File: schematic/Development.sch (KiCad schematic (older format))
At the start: 104 parts

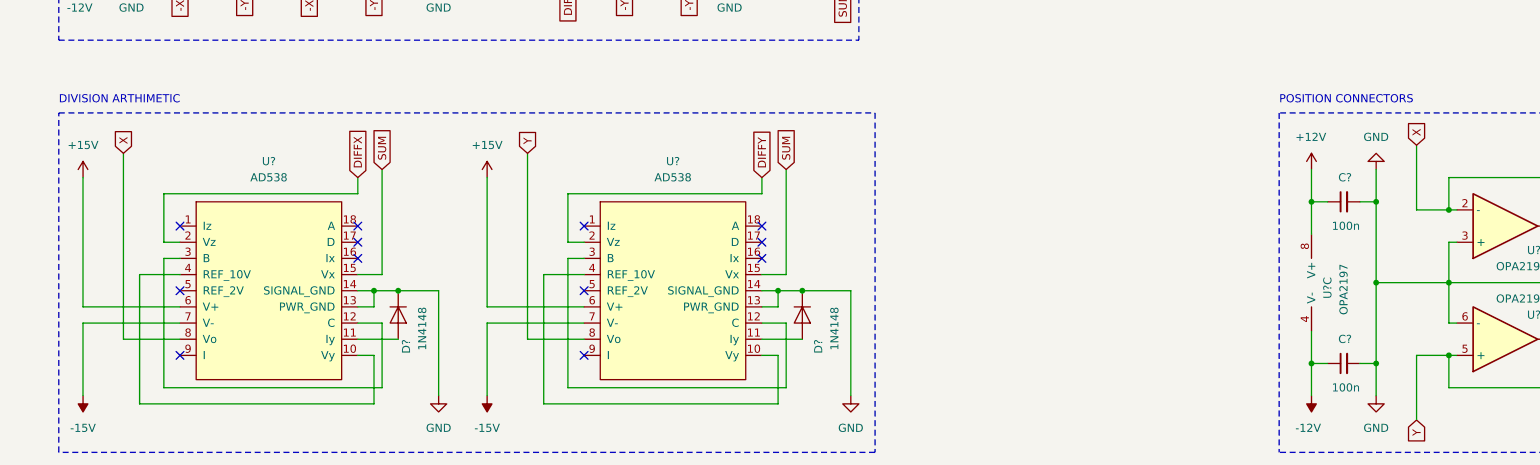
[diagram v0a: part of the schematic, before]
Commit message: renamed X,Y to POSX, POSY
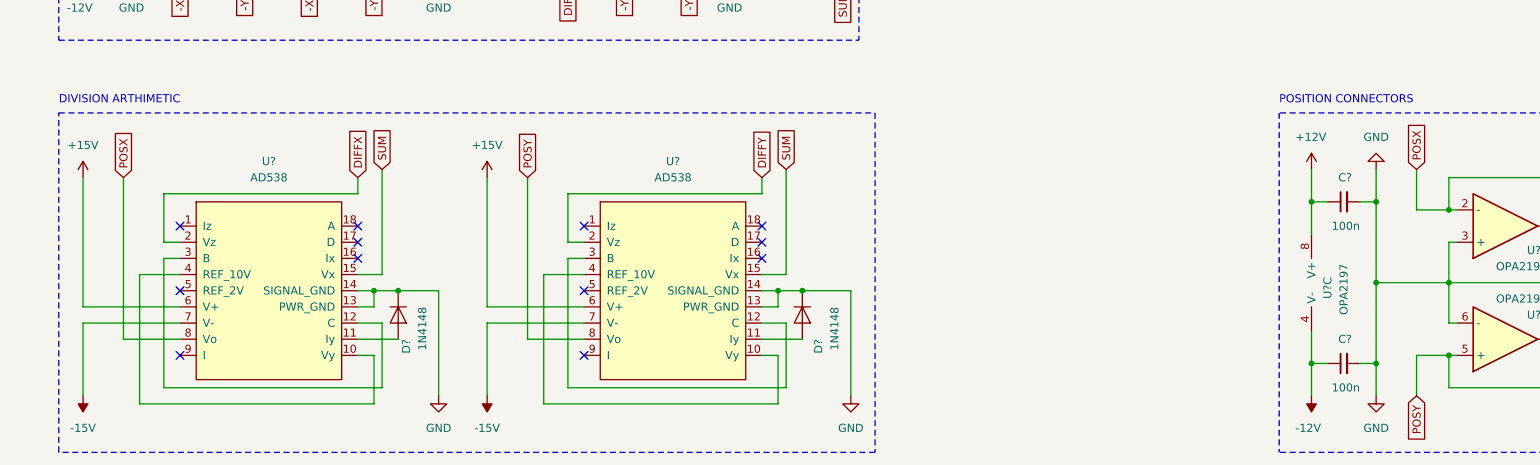
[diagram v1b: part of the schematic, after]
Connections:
- net X renamed POSX
- net Y renamed POSY
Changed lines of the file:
@@
 Wire Wire Line
 	4800 8300 4800 8600
-Text GLabel 4550 8050 1    50   Input ~ 0
-X
+Text GLabel 4550 8200 1    50   Input ~ 0
+POSX
 Wire Wire Line
 	4550 9200 4900 9200
 Wire Wire Line
-	4550 8050 4550 9200
+	4550 8200 4550 9200
 Connection ~ 6250 8900
 Wire Wire Line
@@
 Wire Wire Line
 	7300 8300 7300 8600
-Text GLabel 7050 8050 1    50   Input ~ 0
-Y
+Text GLabel 7050 8200 1    50   Input ~ 0
+POSY
 Wire Wire Line
 	7050 9200 7400 9200
 Wire Wire Line
-	7050 8050 7050 9200
+	7050 8200 7050 9200
 Connection ~ 8750 8900
 Wire Wire Line
@@
 $EndComp
 Wire Wire Line
-	12550 8400 12550 8000
+	12550 8400 12550 8150
 $Comp
 L Connector:Conn_Coaxial J?
@@
 	12550 8400 12750 8400
 Wire Wire Line
-	12550 9300 12550 9700
+	12550 9300 12550 9550
 $Comp
 L Connector:Conn_Coaxial J?
@@
 Wire Notes Line
 	15900 9900 11700 9900
-Text GLabel 12550 8000 1    50   Input ~ 0
-X
-Text GLabel 12550 9700 3    50   Input ~ 0
-Y
+Text GLabel 12550 8150 1    50   Input ~ 0
+POSX
+Text GLabel 12550 9550 3    50   Input ~ 0
+POSY
 $Comp
 L Development-rescue:Opamp_Dual_Generic-Device U?

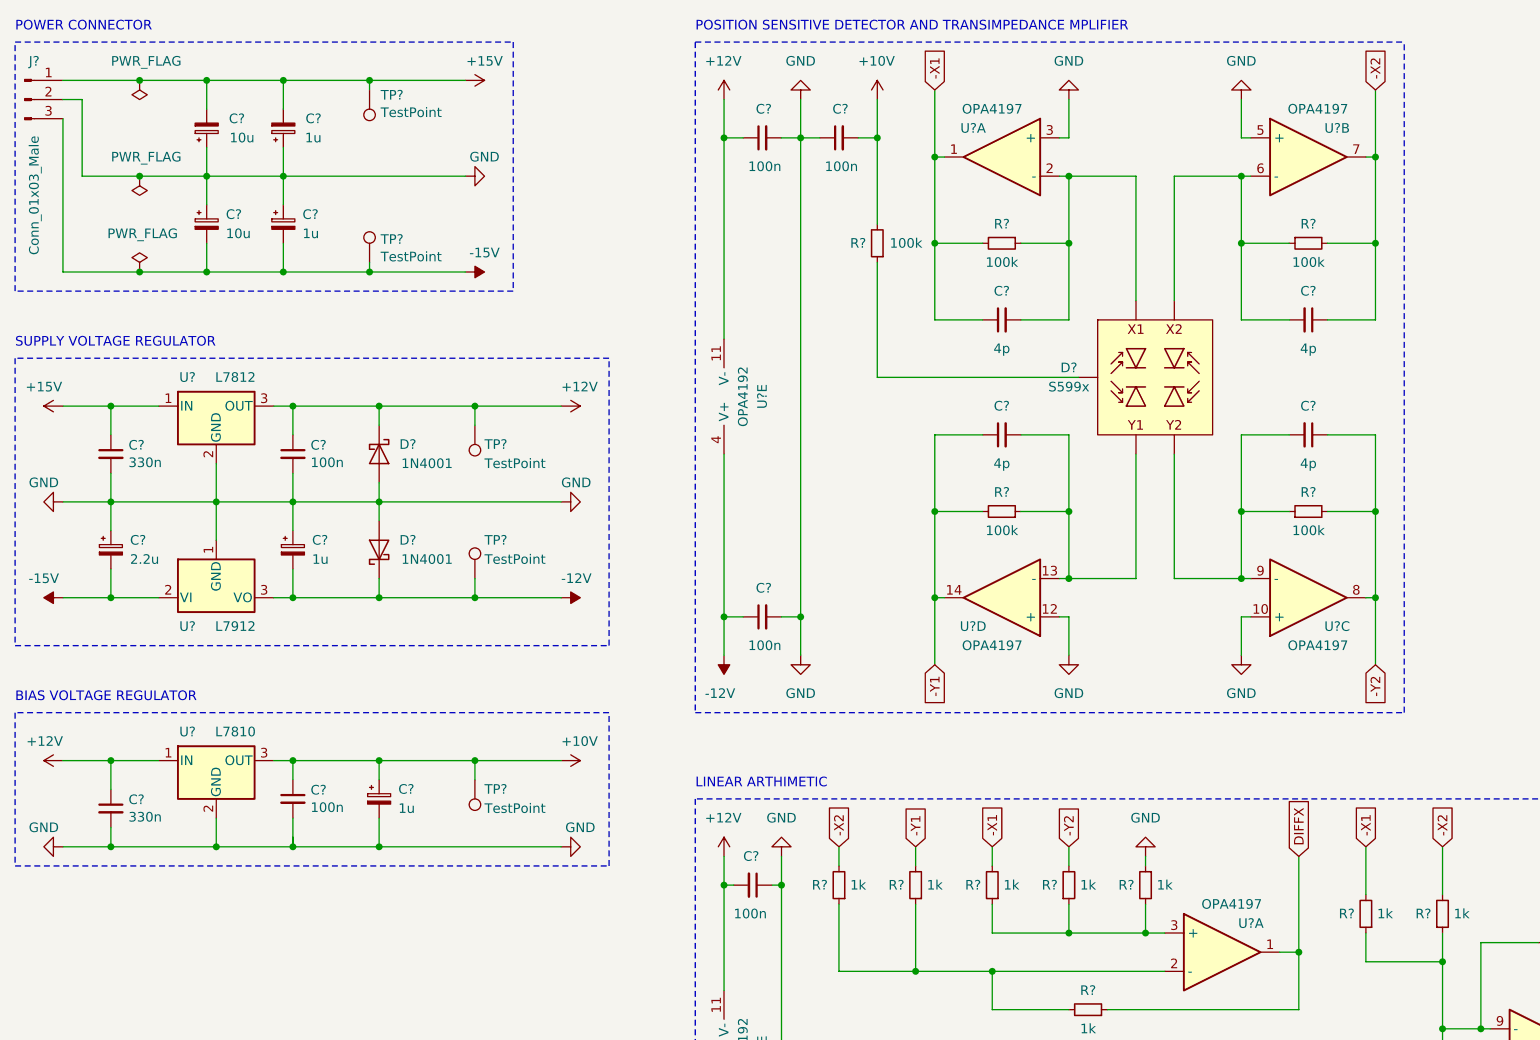
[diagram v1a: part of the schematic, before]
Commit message: replaced reverse bias voltage regulator with voltage reference
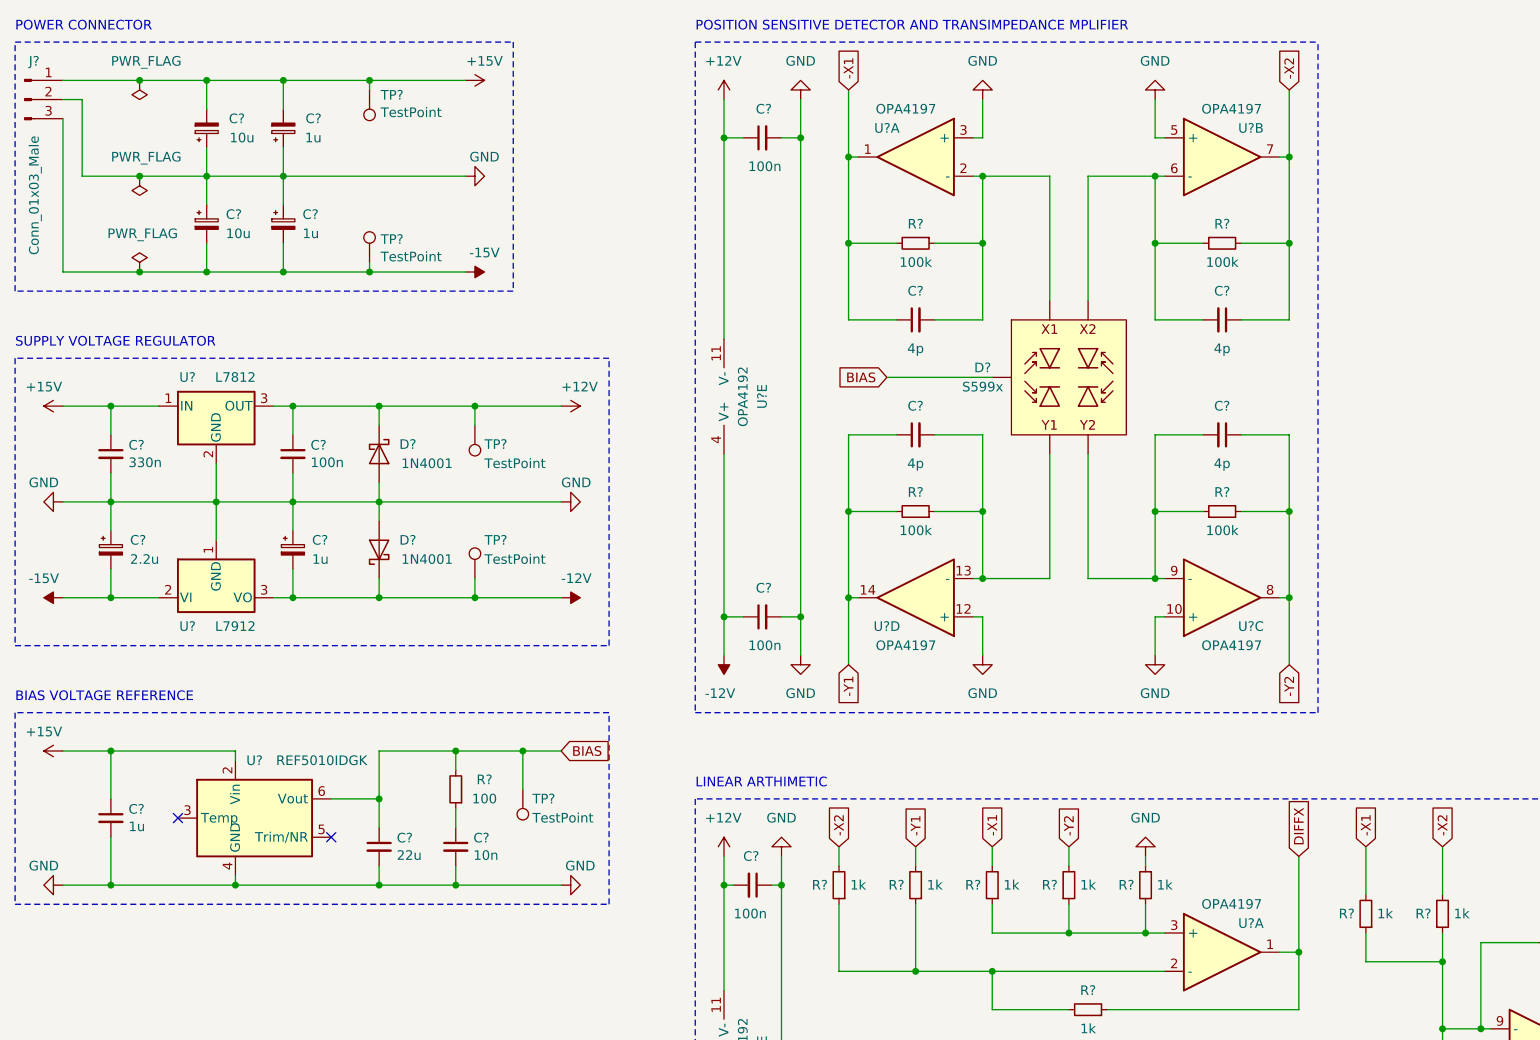
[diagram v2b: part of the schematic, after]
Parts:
- removed C?: 330n, symbol Development-rescue:C_Small-Device
- removed C? (x2): 100n, symbol Development-rescue:C_Small-Device
- removed C?: 1u, symbol Development-rescue:CP_Small-Device
- removed R?: 100k, symbol Development-rescue:R_Small-Device
- removed TP?: TestPoint, symbol Development-rescue:TestPoint-Connector
- removed U?: L7810, symbol Regulator_Linear:L7809
- added C?: 1u, symbol Development-rescue:C_Small-Device
- added C?: 22u, symbol Development-rescue:C_Small-Device
- added C?: 10n, symbol Development-rescue:C_Small-Device
- added R?: 100, symbol Development-rescue:R_Small-Device
- added TP?: TestPoint, symbol Development-rescue:TestPoint-Connector
- added U?: REF5010IDGK, Package_SO:MSOP-8_3x3mm_P0.65mm, symbol Reference_Voltage:REF5010IDGK
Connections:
- net +15V: now also C?.1, U?.2 (Vin)
- net GND: now also C?.2, C?.2, C?.2, U?.4 (GND)
- net BIAS: now reaches D?.8 (K)
- net BIAS: now also C?.1, R?.2, TP?.1, U?.6 (Vout)
- new net: C?.1, R?.1
- no-connect marks 12 -> 14
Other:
- note added: "BIAS VOLTAGE REFERENCE"
- note removed: "BIAS VOLTAGE REGULATOR"
- moved on the sheet: C?, D?, R?, U?A, U?B, U?C, U?D

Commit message: redrew schematic for improved readability, fixed output buffers
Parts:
- removed C? (x4): 100n, symbol Development-rescue:C_Small-Device
- removed D?: 1N4148, Diode_THT:D_DO-35_SOD27_P7.62mm_Horizontal, symbol Diode:1N4148
- removed J?: X1, symbol Connector:Conn_Coaxial
- removed J?: X2, symbol Connector:Conn_Coaxial
- removed J?: Y1, symbol Connector:Conn_Coaxial
- removed J?: Y2, symbol Connector:Conn_Coaxial
- removed J?: DIFFX, symbol Connector:Conn_Coaxial
- removed J?: SUM, symbol Connector:Conn_Coaxial
- removed J?: DIFFY, symbol Connector:Conn_Coaxial
- removed J?: X, symbol Connector:Conn_Coaxial
- removed J?: Y, symbol Connector:Conn_Coaxial
- removed R? (x15): 1k, symbol Development-rescue:R_Small-Device
- removed R? (x7): 50, symbol Development-rescue:R_Small-Device
- removed U? (x6): OPA4197, symbol Development-rescue:Opamp_Quad_Generic-Device
- removed U?: OPA4192, symbol Development-rescue:Opamp_Quad_Generic-Device
- removed U?: AD538, symbol Library:AD538
- added C? (x4): 100n, symbol Development-rescue:C_Small-Device
- added D?: 1N4148, Diode_THT:D_DO-35_SOD27_P7.62mm_Horizontal, symbol Diode:1N4148
- added J? (x9): Conn_Coaxial, symbol Connector:Conn_Coaxial
- added R? (x7): 50, symbol Development-rescue:R_Small-Device
- added R? (x15): 1k, symbol Development-rescue:R_Small-Device
- added U? (x3): OPA4197, symbol Device:Opamp_Quad_Generic
- added U? (x5): OPA4197, symbol Development-rescue:Opamp_Quad_Generic-Device
- added U?: OPA4192, symbol Development-rescue:Opamp_Quad_Generic-Device
- added U?: AD538, symbol Library:AD538
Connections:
- net +12V: now also C?.1, C?.1, U?.11 (V-)
- net +15V: now also U?.6 (V+)
- net -12V: now also C?.1, C?.1, U?.4 (V+)
- net -15V: now also U?.7 (V-)
- net -X1: now also R?.2, R?.2, R?.2; no longer R?.2, U?.1
- net -X2: now also R?.2, R?.2, U?.6 (-)
- net -Y1: now also R?.2, R?.2, R?.2, U?.9 (-); no longer R?.2
- net -Y2: now also R?.2, R?.2, R?.2, U?.13 (-)
- net DIFFX: now also U?.3 (+)
- net DIFFY: now also R?.1, U?.2 (Vz), U?.5 (+)
- net GND: now also C?.2, C?.2, C?.2, C?.2, D?.1 (K), J?.2 (Ext), J?.2 (Ext), J?.2 (Ext), J?.2 (Ext), J?.2 (Ext), J?.2 (Ext), J?.2 (Ext), J?.2 (Ext), J?.2 (Ext), R?.1, R?.1, U?.13 (PWR_GND), U?.14 (SIGNAL_GND); no longer U?.3 (+), U?.3 (+), U?.6 (-)
- net POSX: now also U?.3 (+); no longer U?.1, U?.2 (-)
- net POSY: now also U?.8 (Vo); no longer U?.7
- net SUM: now also R?.1, U?.10 (+), U?.15 (Vx)
- net at R?.1, R?.2, U?.2 (-): now also R?.1
- net at R?.2, U?.3 (+): now also R?.1, R?.1
- net at U?.6 (-): now also R?.1, R?.1, R?.2
- net at U?.5 (+): now also R?.1, R?.1, R?.2
- net at U?.9 (-): now also R?.1, R?.1, R?.1, R?.1, R?.2
- net at U?.10 (+): now also R?.2
- net at R?.1: now also J?.1 (In) (x2)
- new net: R?.2, U?.1, U?.3 (+)
- new net: R?.2, U?.5 (+), U?.7
- new net: R?.2, U?.1, U?.2 (-) (x2)
- new net: R?.2, U?.6 (-), U?.7 (x2)
- new net: J?.1 (In), R?.1 (x7)
- new net: R?.2, U?.10 (+), U?.8
- new net: R?.2, U?.12 (+), U?.14
- new net: R?.2, U?.8, U?.9 (-)
- new net: U?.10 (Vy), U?.4 (REF_10V)
- new net: D?.2 (A), U?.11 (Iy)
- new net: U?.12 (C), U?.3 (B)
- no-connect marks 14 -> 20
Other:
- note added: "MEASUREMENT CONNECTORS"
- note added: "POSITION SENSITIVE DETECTOR AND TRANSIMPEDANCE AMPLIFIER"
- note removed: "ANODE TERMINAL CONNECTORS"
- note removed: "POSITION CONNECTORS"
- note removed: "POSITION SENSITIVE DETECTOR AND TRANSIMPEDANCE MPLIFIER"
- note removed: "SUM AND DIFFERENCE CONNECTORS"
- moved on the sheet: C?, D?, J?, R?, TP?, U?, U?A, U?B, U?C, U?D, U?E
